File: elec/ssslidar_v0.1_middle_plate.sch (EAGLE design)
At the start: 6 parts

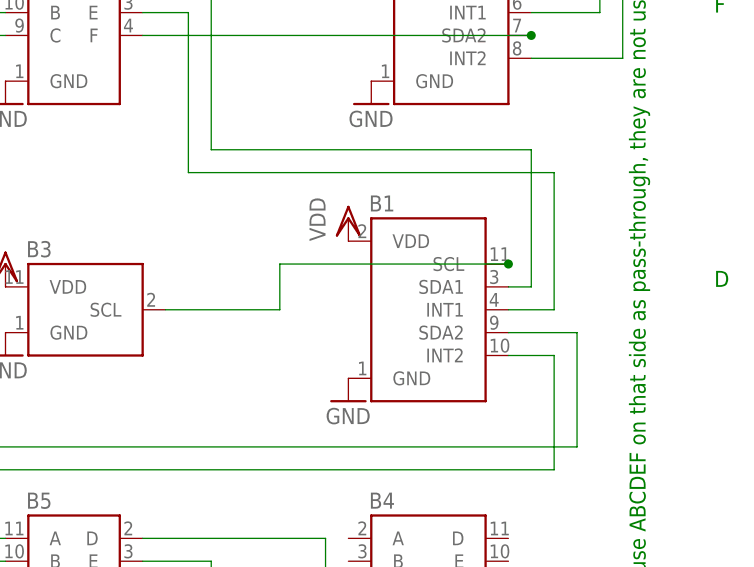
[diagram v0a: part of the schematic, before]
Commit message: Fixed middle plate with double power rails
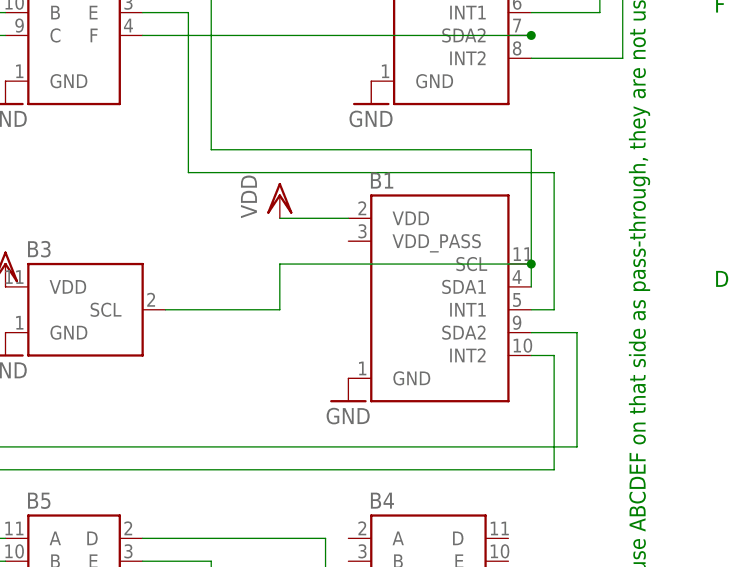
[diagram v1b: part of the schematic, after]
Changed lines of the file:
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@@
 <instance part="GND1" gate="1" x="-2.54" y="63.5"/>
 <instance part="VDD1" gate="G$1" x="-2.54" y="73.66"/>
-<instance part="VDD2" gate="G$1" x="35.56" y="78.74"/>
+<instance part="VDD2" gate="G$1" x="27.94" y="81.28"/>
 <instance part="GND2" gate="1" x="35.56" y="58.42"/>
 <instance part="GND3" gate="1" x="38.1" y="91.44"/>
@@
 <pinref part="B1" gate="G$1" pin="VDD"/>
 <pinref part="VDD2" gate="G$1" pin="VDD"/>
+<wire x1="27.94" y1="78.74" x2="35.56" y2="78.74" width="0.1524" layer="91"/>
 </segment>
 </net>
@@
 <wire x1="27.94" y1="68.58" x2="27.94" y2="73.66" width="0.1524" layer="91"/>
 <pinref part="B1" gate="G$1" pin="SCL"/>
-<wire x1="27.94" y1="73.66" x2="53.34" y2="73.66" width="0.1524" layer="91"/>
-<junction x="53.34" y="73.66"/>
+<wire x1="27.94" y1="73.66" x2="55.88" y2="73.66" width="0.1524" layer="91"/>
+<junction x="55.88" y="73.66"/>
 </segment>
 </net>
@@
 <wire x1="58.42" y1="83.82" x2="58.42" y2="68.58" width="0.1524" layer="91"/>
 <pinref part="B1" gate="G$1" pin="INT1"/>
-<wire x1="58.42" y1="68.58" x2="53.34" y2="68.58" width="0.1524" layer="91"/>
+<wire x1="58.42" y1="68.58" x2="55.88" y2="68.58" width="0.1524" layer="91"/>
 </segment>
 </net>
@@
 <wire x1="60.96" y1="53.34" x2="60.96" y2="66.04" width="0.1524" layer="91"/>
 <pinref part="B1" gate="G$1" pin="SDA2"/>
-<wire x1="60.96" y1="66.04" x2="53.34" y2="66.04" width="0.1524" layer="91"/>
+<wire x1="60.96" y1="66.04" x2="55.88" y2="66.04" width="0.1524" layer="91"/>
 </segment>
 </net>
@@
 <wire x1="58.42" y1="50.8" x2="58.42" y2="63.5" width="0.1524" layer="91"/>
 <pinref part="B1" gate="G$1" pin="INT2"/>
-<wire x1="58.42" y1="63.5" x2="53.34" y2="63.5" width="0.1524" layer="91"/>
+<wire x1="58.42" y1="63.5" x2="55.88" y2="63.5" width="0.1524" layer="91"/>
 </segment>
 </net>
@@
 <segment>
 <pinref part="B1" gate="G$1" pin="SDA1"/>
-<wire x1="53.34" y1="71.12" x2="55.88" y2="71.12" width="0.1524" layer="91"/>
 <wire x1="55.88" y1="71.12" x2="55.88" y2="86.36" width="0.1524" layer="91"/>
 <wire x1="55.88" y1="86.36" x2="20.32" y2="86.36" width="0.1524" layer="91"/>
